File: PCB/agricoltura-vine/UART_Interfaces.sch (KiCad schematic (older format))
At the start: 10 parts

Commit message: Schematic process
scheamtics laid out for all board subsyhstems, connecting MCU to subsystems still in progress, power yet to be designed.
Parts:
- added C? (x2): C0402C104K9PACTU, AVR-KiCAD-Lib-Resistors:R0402, symbol AVR-KiCAD-Lib-Capacitors:C0402C104K9PACTU
- added C? (x2): GRM188R61A106KE69J, AVR-KiCAD-Lib-Capacitors:C0603, symbol AVR-KiCAD-Lib-Capacitors:GRM188R61A106KE69J
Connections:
- net labels added: +3V3, GND, UART_SENSE1_RX, UART_SENSE1_TX, UART_SENSE2_RX, UART_SENSE2_TX, USW1_EN, USW1_S0, USW1_S1, USW2_EN, USW2_S0, USW2_S1
- wire segments 48 -> 77
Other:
- moved on the sheet: U?

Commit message: 5V Logic, Connector swap, and I2C refactor
Added 5V IO logic, changed connectors over to grove style SMT, I2C refactored to use 8x mux instead fo two 4x mux.
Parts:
- removed T? (x8): 0705430003, AVR-KiCAD-Lib-Connectors:Shrouded_Pin_Header_Straight_1x04_Pitch2.54mm, symbol AVR-KiCAD-Lib-Connectors:0705430003
- added T? (x8): BM04B-SRSS-TB(LF)(SN), AVR-KiCAD-Lib-Connectors:CONN_BM04B-SRSS-TB(LF)(SN), symbol AVR-KiCAD-Lib-Connectors:BM04B-SRSS-TB(LF)(SN)
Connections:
- wire segments 77 -> 109
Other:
- moved on the sheet: C?, U?

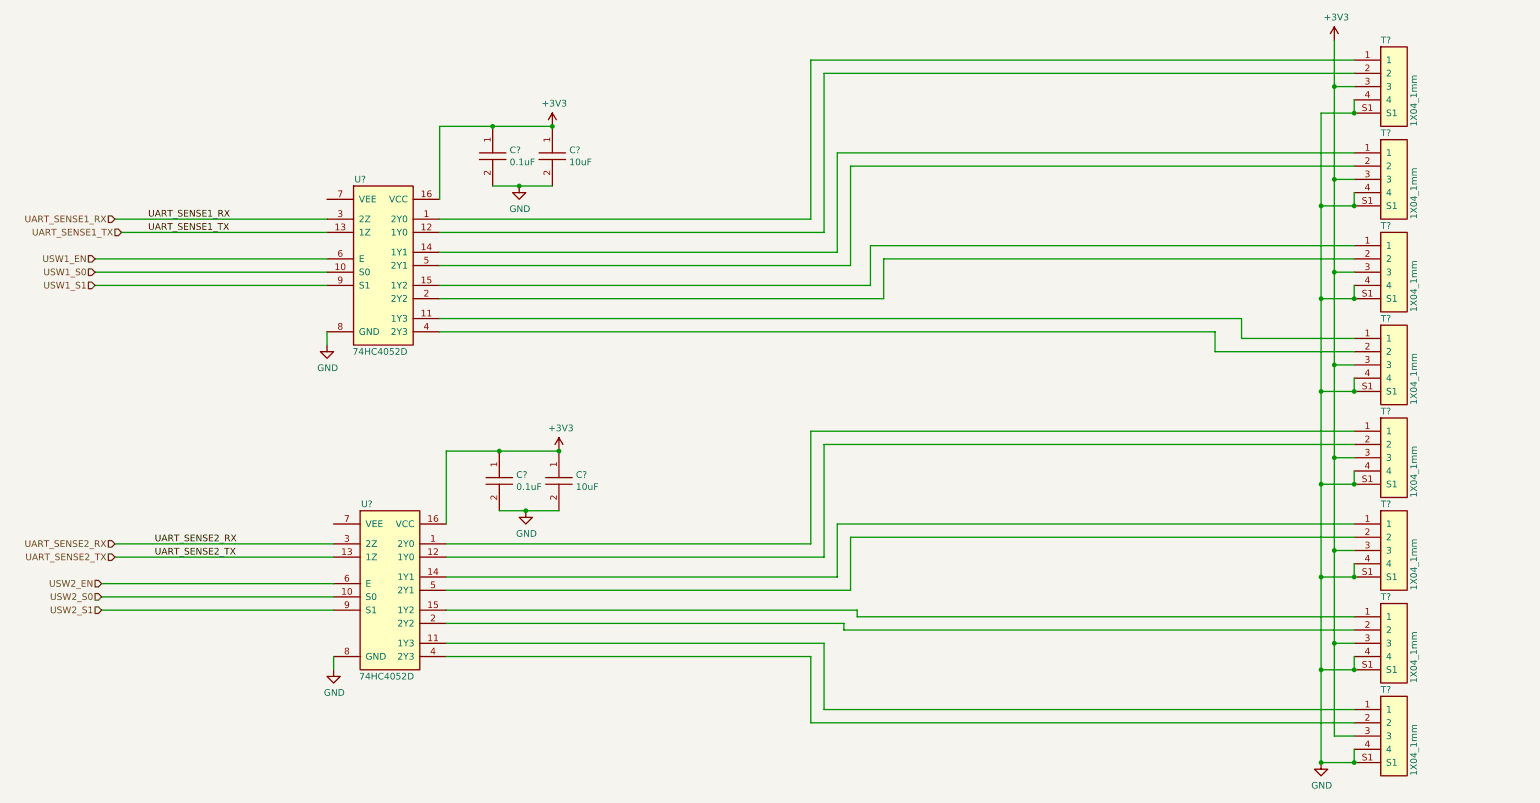
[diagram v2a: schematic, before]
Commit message: Schematic Pass 1
All subsystem schematics are completed in their first pass, some features scaled back to make design more practical.
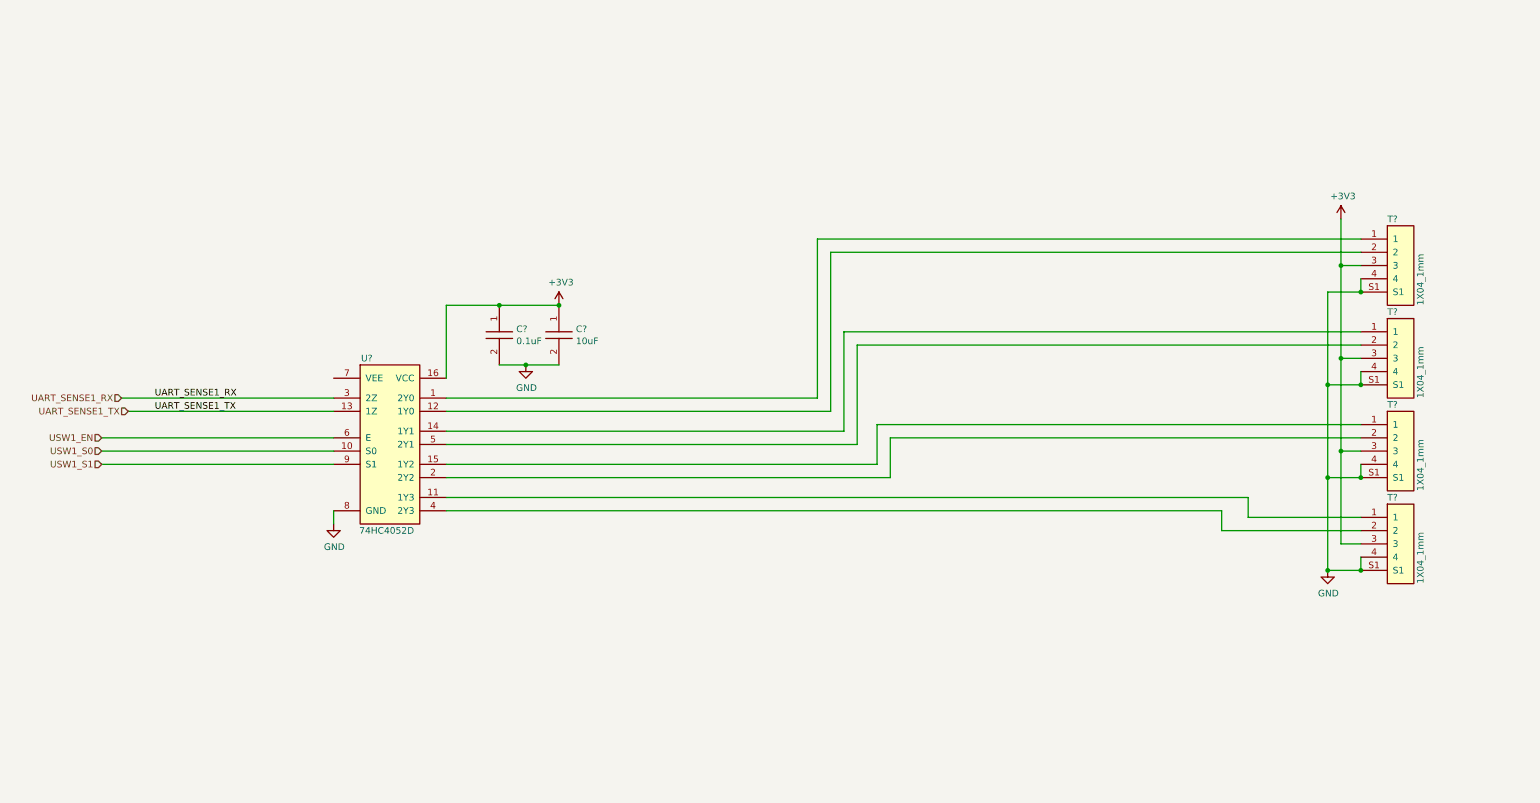
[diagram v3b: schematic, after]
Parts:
- removed C?: C0402C104K9PACTU, AVR-KiCAD-Lib-Resistors:R0402, symbol AVR-KiCAD-Lib-Capacitors:C0402C104K9PACTU
- removed C?: GRM188R61A106KE69J, AVR-KiCAD-Lib-Capacitors:C0603, symbol AVR-KiCAD-Lib-Capacitors:GRM188R61A106KE69J
- removed T? (x4): BM04B-SRSS-TB(LF)(SN), AVR-KiCAD-Lib-Connectors:CONN_BM04B-SRSS-TB(LF)(SN), symbol AVR-KiCAD-Lib-Connectors:BM04B-SRSS-TB(LF)(SN)
- removed U?: 74HC4052D, AVR-KiCAD-Lib-ICs:74HC4052D, symbol AVR-KiCAD-Lib-ICs:74HC4052D
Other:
- moved on the sheet: C?, T?, U?

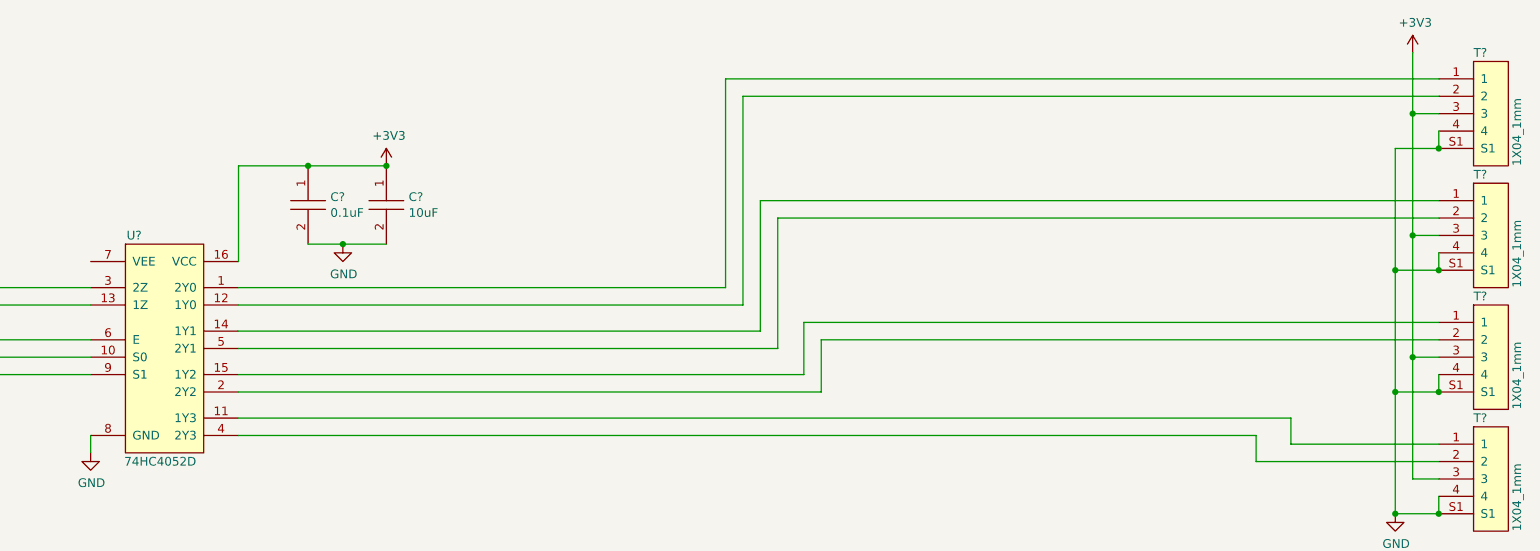
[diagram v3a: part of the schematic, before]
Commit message: Board
Board shape defined, though subject to change. Schematic anotated and parts exported to board.
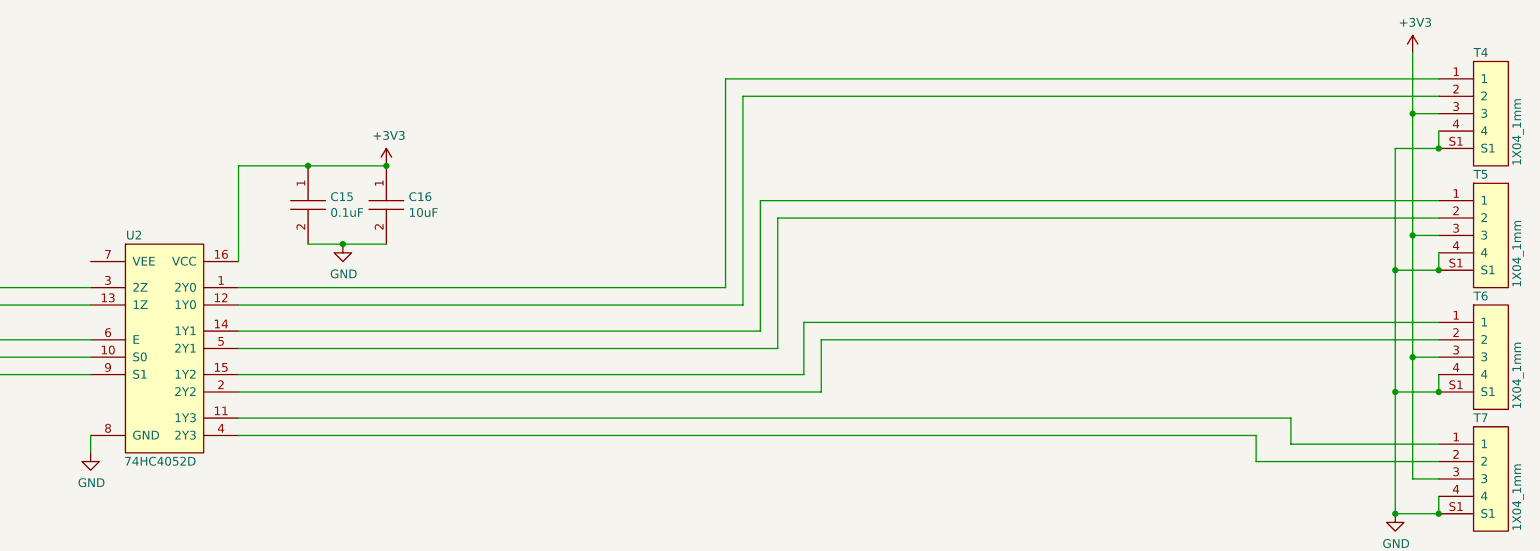
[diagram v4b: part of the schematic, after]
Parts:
- gave numbers to parts that had none: 7
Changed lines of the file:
@@
 $EndDescr
 $Comp
-L AVR-KiCAD-Lib-ICs:74HC4052D U?
+L AVR-KiCAD-Lib-ICs:74HC4052D U2
 U 1 1 5EFDBFF8
 P 3050 3250
-F 0 "U?" H 3100 3300 50  0000 C CNN
+F 0 "U2" H 3100 3300 50  0000 C CNN
 F 1 "74HC4052D" H 3100 3450 50  0001 C CNN
 F 2 "AVR-KiCAD-Lib-ICs:74HC4052D" H 2850 3200 50  0001 C CNN
@@
 P 4100 3000
 AR Path="/5EE82896/5F137C30" Ref="C?"  Part="1"
-AR Path="/5EE82702/5F137C30" Ref="C?"  Part="1"
-F 0 "C?" V 4079 3128 50  0000 L CNN
+AR Path="/5EE82702/5F137C30" Ref="C15"  Part="1"
+F 0 "C15" V 4079 3128 50  0000 L CNN
 F 1 "C0402C104K9PACTU" H 4150 3200 50  0001 C CNN
 F 2 "AVR-KiCAD-Lib-Resistors:R0402" H 3900 3000 50  0001 C CNN
@@
 P 4550 3000
 AR Path="/5EE82896/5F137C4F" Ref="C?"  Part="1"
-AR Path="/5EE82702/5F137C4F" Ref="C?"  Part="1"
-F 0 "C?" V 4529 3128 50  0000 L CNN
+AR Path="/5EE82702/5F137C4F" Ref="C16"  Part="1"
+F 0 "C16" V 4529 3128 50  0000 L CNN
 F 1 "GRM188R61A106KE69J" H 4600 3200 50  0001 C CNN
 F 2 "AVR-KiCAD-Lib-Capacitors:C0603" H 4350 3000 50  0001 C CNN
@@
 P 4550 2800
 AR Path="/5EE82896/5F137C58" Ref="#PWR?"  Part="1"
-AR Path="/5EE82702/5F137C58" Ref="#PWR?"  Part="1"
-F 0 "#PWR?" H 4550 2650 50  0001 C CNN
+AR Path="/5EE82702/5F137C58" Ref="#PWR021"  Part="1"
+F 0 "#PWR021" H 4550 2650 50  0001 C CNN
 F 1 "+3V3" H 4565 2973 50  0000 C CNN
 F 2 "" H 4550 2800 50  0001 C CNN
@@
 P 4300 3250
 AR Path="/5EE82896/5F137C62" Ref="#PWR?"  Part="1"
-AR Path="/5EE82702/5F137C62" Ref="#PWR?"  Part="1"
-F 0 "#PWR?" H 4300 3000 50  0001 C CNN
+AR Path="/5EE82702/5F137C62" Ref="#PWR020"  Part="1"
+F 0 "#PWR020" H 4300 3000 50  0001 C CNN
 F 1 "GND" H 4305 3077 50  0000 C CNN
 F 2 "" H 4300 3250 50  0001 C CNN
@@
 $EndComp
 $Comp
-L power:GND #PWR?
+L power:GND #PWR019
 U 1 1 5F13C4D0
 P 2850 4450
-F 0 "#PWR?" H 2850 4200 50  0001 C CNN
+F 0 "#PWR019" H 2850 4200 50  0001 C CNN
 F 1 "GND" H 2855 4277 50  0000 C CNN
 F 2 "" H 2850 4450 50  0001 C CNN
@@
 P 10450 2150
 AR Path="/5EE82896/5F151E2B" Ref="#PWR?"  Part="1"
-AR Path="/5EE82702/5F151E2B" Ref="#PWR?"  Part="1"
-F 0 "#PWR?" H 10450 2000 50  0001 C CNN
+AR Path="/5EE82702/5F151E2B" Ref="#PWR023"  Part="1"
+F 0 "#PWR023" H 10450 2000 50  0001 C CNN
 F 1 "+3V3" H 10465 2323 50  0000 C CNN
 F 2 "" H 10450 2150 50  0001 C CNN
@@
 	2850 4000 1100 4000
 $Comp
-L AVR-KiCAD-Lib-Connectors:BM04B-SRSS-TB(LF)(SN) T?
+L AVR-KiCAD-Lib-Connectors:BM04B-SRSS-TB(LF)(SN) T4
 U 1 1 5EFE95D1
 P 10800 2200
-F 0 "T?" H 10800 2250 50  0000 L CNN
+F 0 "T4" H 10800 2250 50  0000 L CNN
 F 1 "BM04B-SRSS-TB(LF)(SN)" H 10850 2400 50  0001 C CNN
 F 2 "AVR-KiCAD-Lib-Connectors:CONN_BM04B-SRSS-TB(LF)(SN)" H 9900 2800 50  0001 C CNN
@@
 $EndComp
 $Comp
-L AVR-KiCAD-Lib-Connectors:BM04B-SRSS-TB(LF)(SN) T?
+L AVR-KiCAD-Lib-Connectors:BM04B-SRSS-TB(LF)(SN) T5
 U 1 1 5EFECB6B
 P 10800 2900
-F 0 "T?" H 10800 2950 50  0000 L CNN
+F 0 "T5" H 10800 2950 50  0000 L CNN
 F 1 "BM04B-SRSS-TB(LF)(SN)" H 10850 3100 50  0001 C CNN
 F 2 "AVR-KiCAD-Lib-Connectors:CONN_BM04B-SRSS-TB(LF)(SN)" H 9900 3500 50  0001 C CNN
@@
 $EndComp
 $Comp
-L AVR-KiCAD-Lib-Connectors:BM04B-SRSS-TB(LF)(SN) T?
+L AVR-KiCAD-Lib-Connectors:BM04B-SRSS-TB(LF)(SN) T6
 U 1 1 5EFED7B2
 P 10800 3600
-F 0 "T?" H 10800 3650 50  0000 L CNN
+F 0 "T6" H 10800 3650 50  0000 L CNN
 F 1 "BM04B-SRSS-TB(LF)(SN)" H 10850 3800 50  0001 C CNN
 F 2 "AVR-KiCAD-Lib-Connectors:CONN_BM04B-SRSS-TB(LF)(SN)" H 9900 4200 50  0001 C CNN
@@
 $EndComp
 $Comp
-L AVR-KiCAD-Lib-Connectors:BM04B-SRSS-TB(LF)(SN) T?
+L AVR-KiCAD-Lib-Connectors:BM04B-SRSS-TB(LF)(SN) T7
 U 1 1 5EFEE98D
 P 10800 4300
-F 0 "T?" H 10800 4350 50  0000 L CNN
+F 0 "T7" H 10800 4350 50  0000 L CNN
 F 1 "BM04B-SRSS-TB(LF)(SN)" H 10850 4500 50  0001 C CNN
 F 2 "AVR-KiCAD-Lib-Connectors:CONN_BM04B-SRSS-TB(LF)(SN)" H 9900 4900 50  0001 C CNN
@@
 	3700 4100 7050 4100
 $Comp
-L power:GND #PWR?
+L power:GND #PWR022
 U 1 1 5F0D61E7
 P 10350 4800
-F 0 "#PWR?" H 10350 4550 50  0001 C CNN
+F 0 "#PWR022" H 10350 4550 50  0001 C CNN
 F 1 "GND" H 10355 4627 50  0000 C CNN
 F 2 "" H 10350 4800 50  0001 C CNN

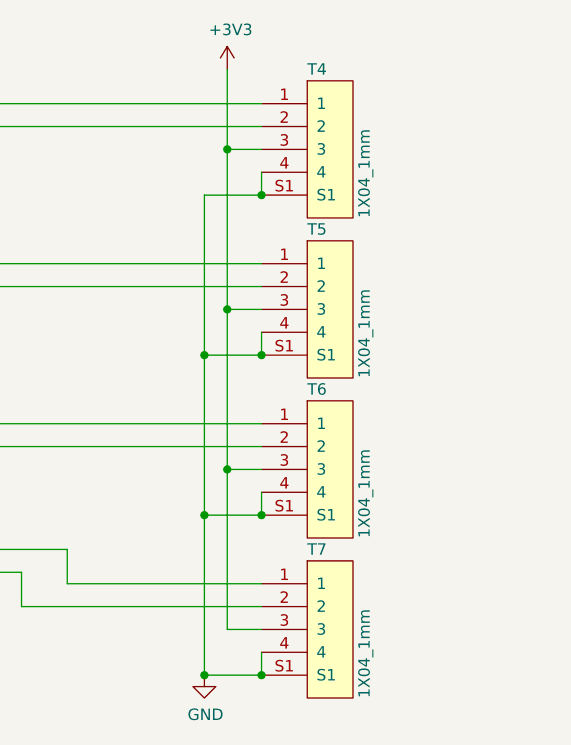
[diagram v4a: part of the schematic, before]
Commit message: Board shape and Rough PLacement
Board shape adjusted to have smaller rounded corners increasing usable space of board shape. Finished rough placement of all the components, no routing yet. Debating connector style and form factor. Right now supports Seeedstudio grove connectors, contemplating Sparkfun Qwiic  and Adafruit Stemma connectors as alternatives or including a variety of all 3.
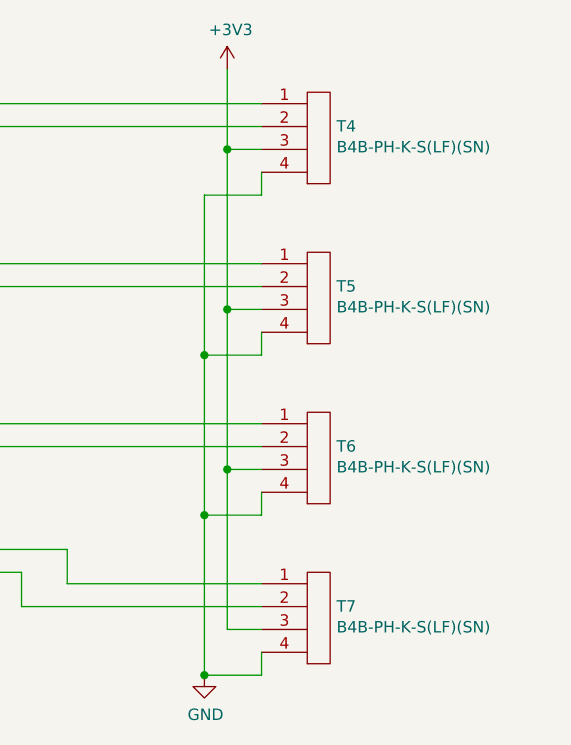
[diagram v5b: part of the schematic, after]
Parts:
- removed T4, T5, T6, T7: BM04B-SRSS-TB(LF)(SN), AVR-KiCAD-Lib-Connectors:CONN_BM04B-SRSS-TB(LF)(SN), symbol AVR-KiCAD-Lib-Connectors:BM04B-SRSS-TB(LF)(SN)
- added T4, T5, T6, T7: B4B-PH-K-S(LF)(SN), AVR-KiCAD-Lib-Connectors:B4B-PH-K-S(LF)(SN), symbol AVR-KiCAD-Lib-Connectors:B4B-PH-K-S(LF)(SN)
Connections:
- net +3V3: now also T4.3, T5.3, T6.3, T7.3
- net GND: now also T4.4, T5.4, T6.4, T7.4
- net at U2.1 (2Y0): now also T4.1
- net at U2.11 (1Y3): now also T7.1
- net at U2.12 (1Y0): now also T4.2
- net at U2.14 (1Y1): now also T5.1
- net at U2.15 (1Y2): now also T6.1
- net at U2.2 (2Y2): now also T6.2
- net at U2.4 (2Y3): now also T7.2
- net at U2.5 (2Y1): now also T5.2

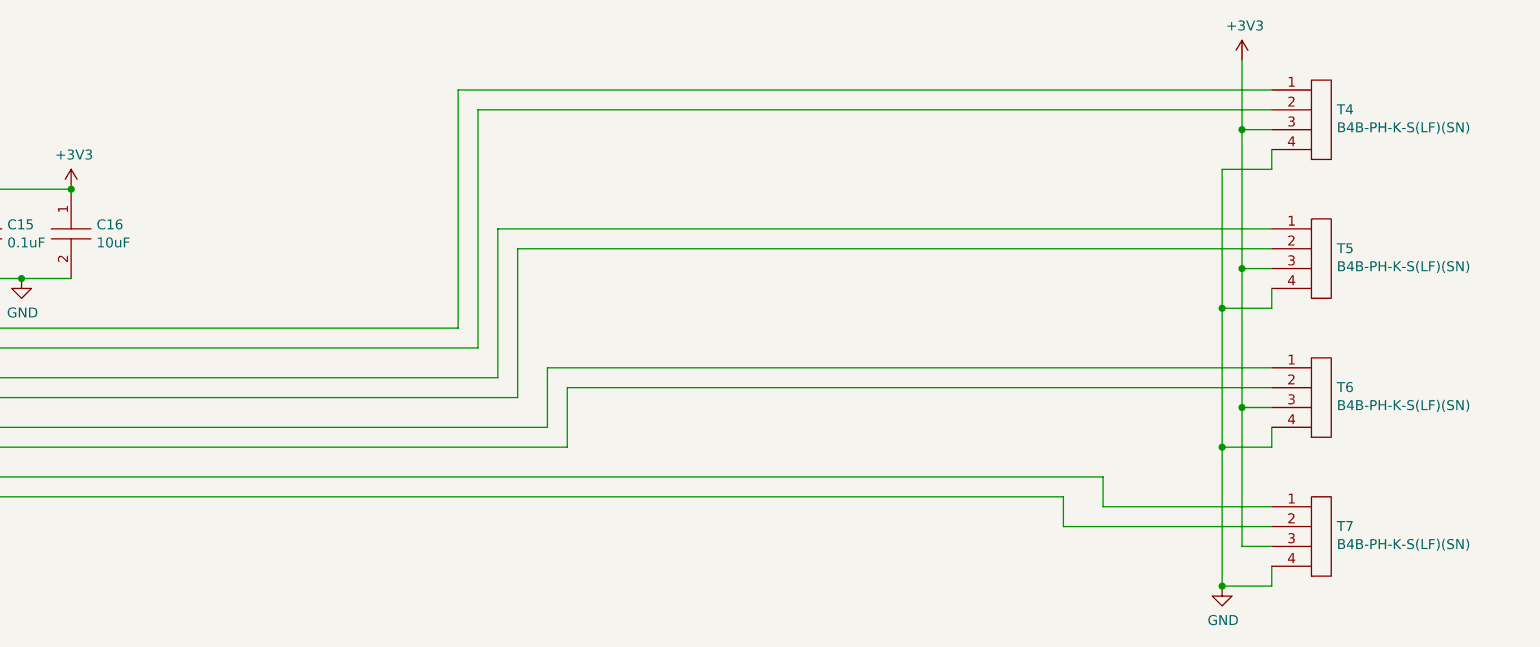
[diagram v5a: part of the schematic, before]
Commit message: Route Started Connectors Changed
Changed to QWIIC style connectors and adjusted pinning of RJ45s, but switching to screw terminal header in next commit. THis is a backup
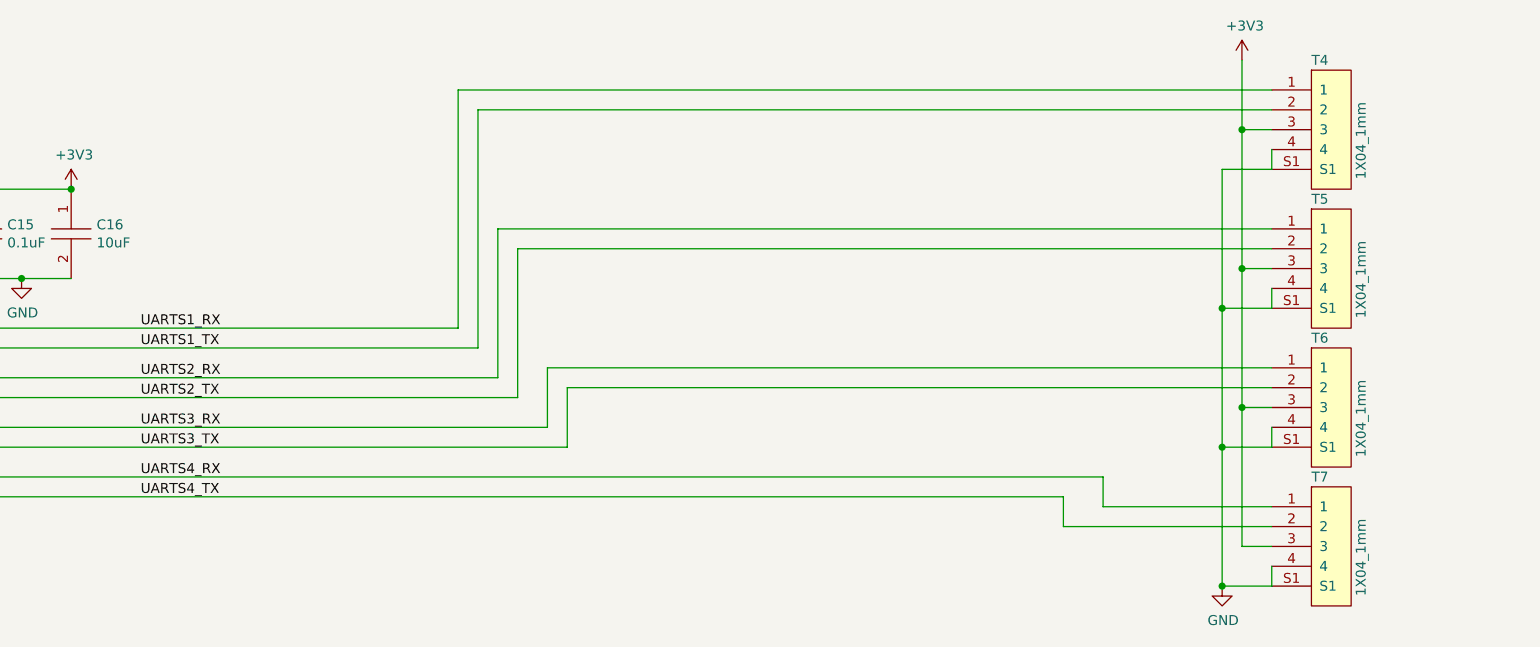
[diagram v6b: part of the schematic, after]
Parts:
- removed T4, T5, T6, T7: B4B-PH-K-S(LF)(SN), AVR-KiCAD-Lib-Connectors:B4B-PH-K-S(LF)(SN), symbol AVR-KiCAD-Lib-Connectors:B4B-PH-K-S(LF)(SN)
- added T4, T5, T6, T7: BM04B-SRSS-TB(LF)(SN), AVR-KiCAD-Lib-Connectors:CONN_BM04B-SRSS-TB(LF)(SN), symbol AVR-KiCAD-Lib-Connectors:BM04B-SRSS-TB(LF)(SN)
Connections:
- net +3V3: now also T4.3, T5.3, T6.3, T7.3
- net GND: now also T4.4, T4.S1, T5.4, T5.S1, T6.4, T6.S1, T7.4, T7.S1
- net UARTS1_RX: now reaches U2.1 (2Y0)
- net UARTS1_RX: now also T4.1
- net UARTS1_TX: now reaches U2.12 (1Y0)
- net UARTS1_TX: now also T4.2
- net UARTS2_RX: now reaches U2.14 (1Y1)
- net UARTS2_RX: now also T5.1
- net UARTS2_TX: now reaches U2.5 (2Y1)
- net UARTS2_TX: now also T5.2
- net UARTS3_RX: now reaches U2.15 (1Y2)
- net UARTS3_RX: now also T6.1
- net UARTS3_TX: now reaches U2.2 (2Y2)
- net UARTS3_TX: now also T6.2
- net UARTS4_RX: now reaches U2.11 (1Y3)
- net UARTS4_RX: now also T7.1
- net UARTS4_TX: now reaches U2.4 (2Y3)
- net UARTS4_TX: now also T7.2
